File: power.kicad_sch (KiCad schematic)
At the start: 32 parts

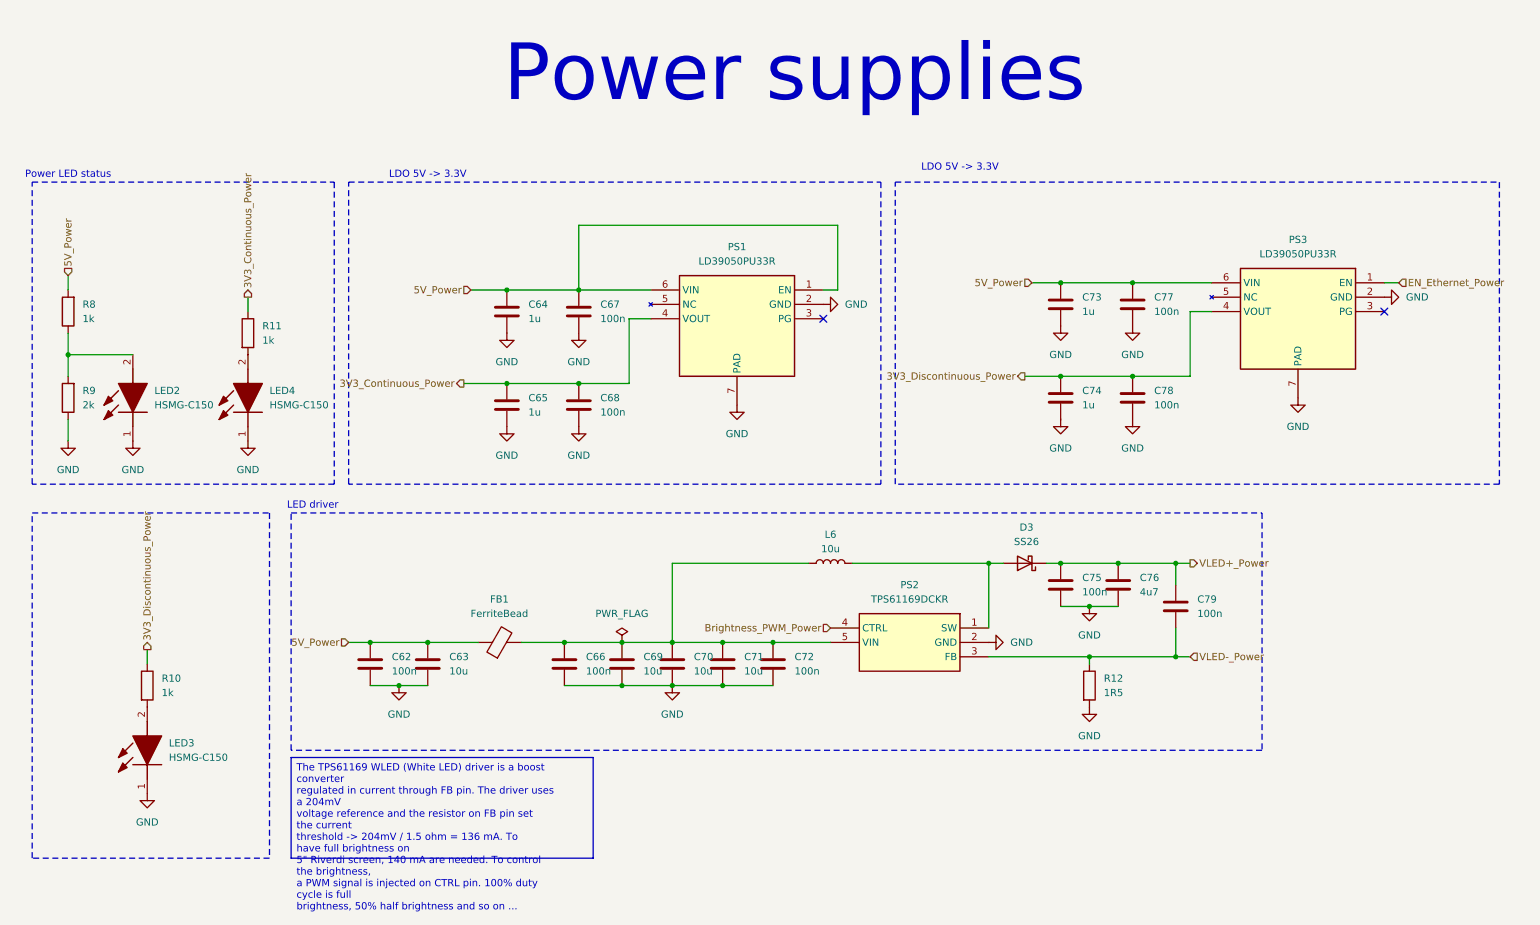
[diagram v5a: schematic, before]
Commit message: Remove Ethernet part, critical error, LAN8651 is 10BASE-T1S !
10BASE-T1S is not suitable with RJ45 connector and not connectable to computer
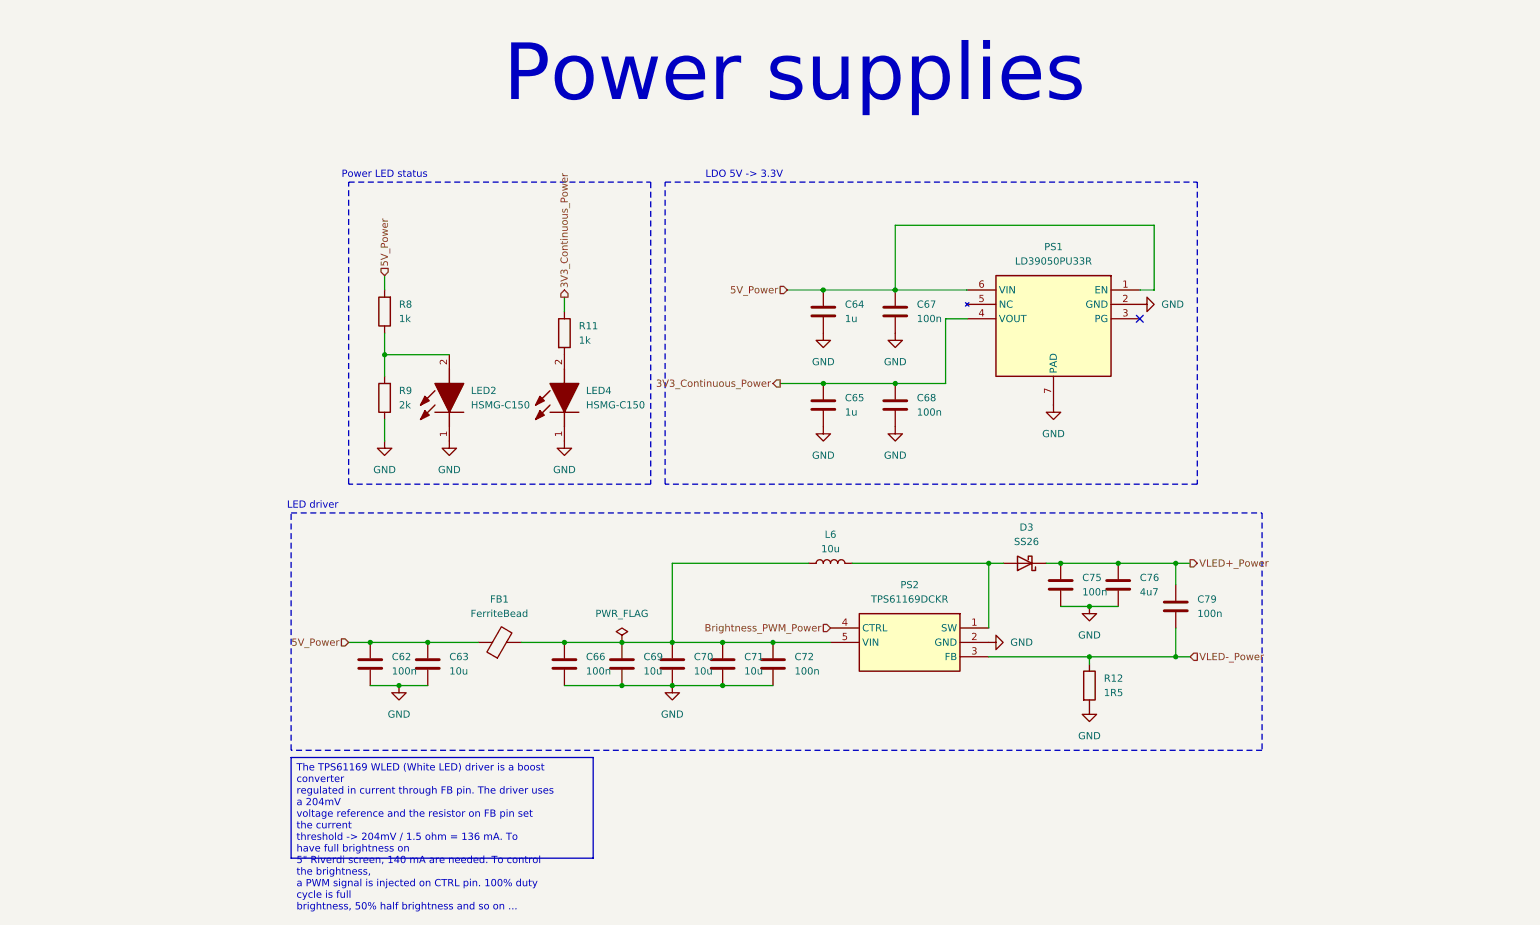
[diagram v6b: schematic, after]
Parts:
- removed C73, C74: 1u, symbol Device:C
- removed C77, C78: 100n, symbol Device:C
- removed LED3: HSMG-C150, weather-station-poc-fp:LEDC3216X120N, symbol weather-station-poc-sym:HSMG-C150
- removed PS3: LD39050PU33R, weather-station-poc-fp:SON95P300X300X100-7N-D, symbol weather-station-poc-sym:LD39050PU33R
- removed R10: 1k, symbol Device:R
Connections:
- no-connect marks 2 -> 1
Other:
- moved on the sheet: C64, C65, C67, C68, LED2, LED4, PS1, R11, R8, R9

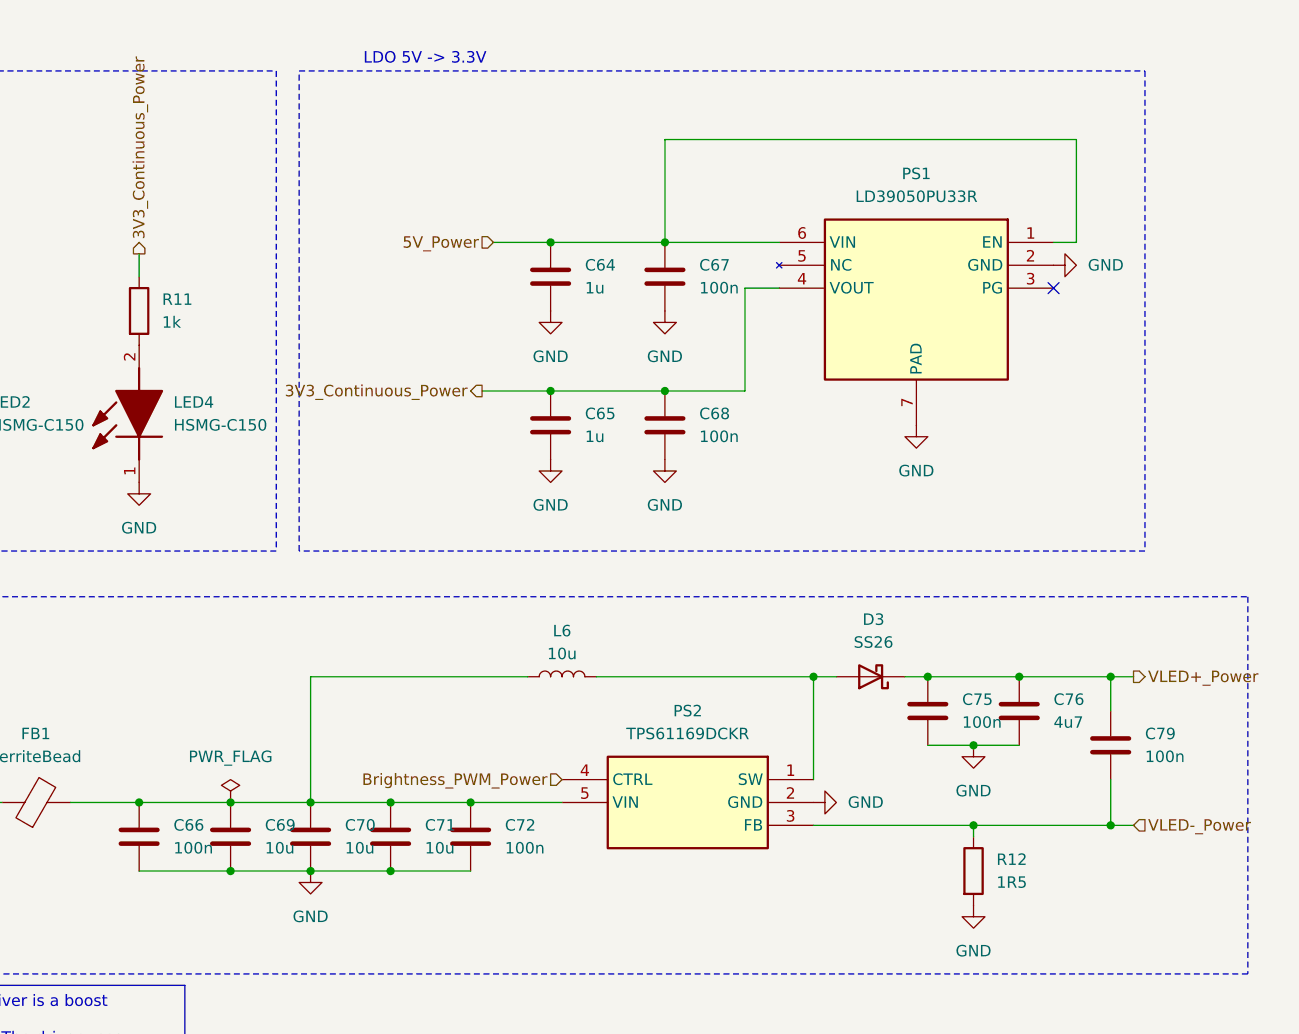
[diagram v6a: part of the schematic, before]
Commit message: Reorder components number
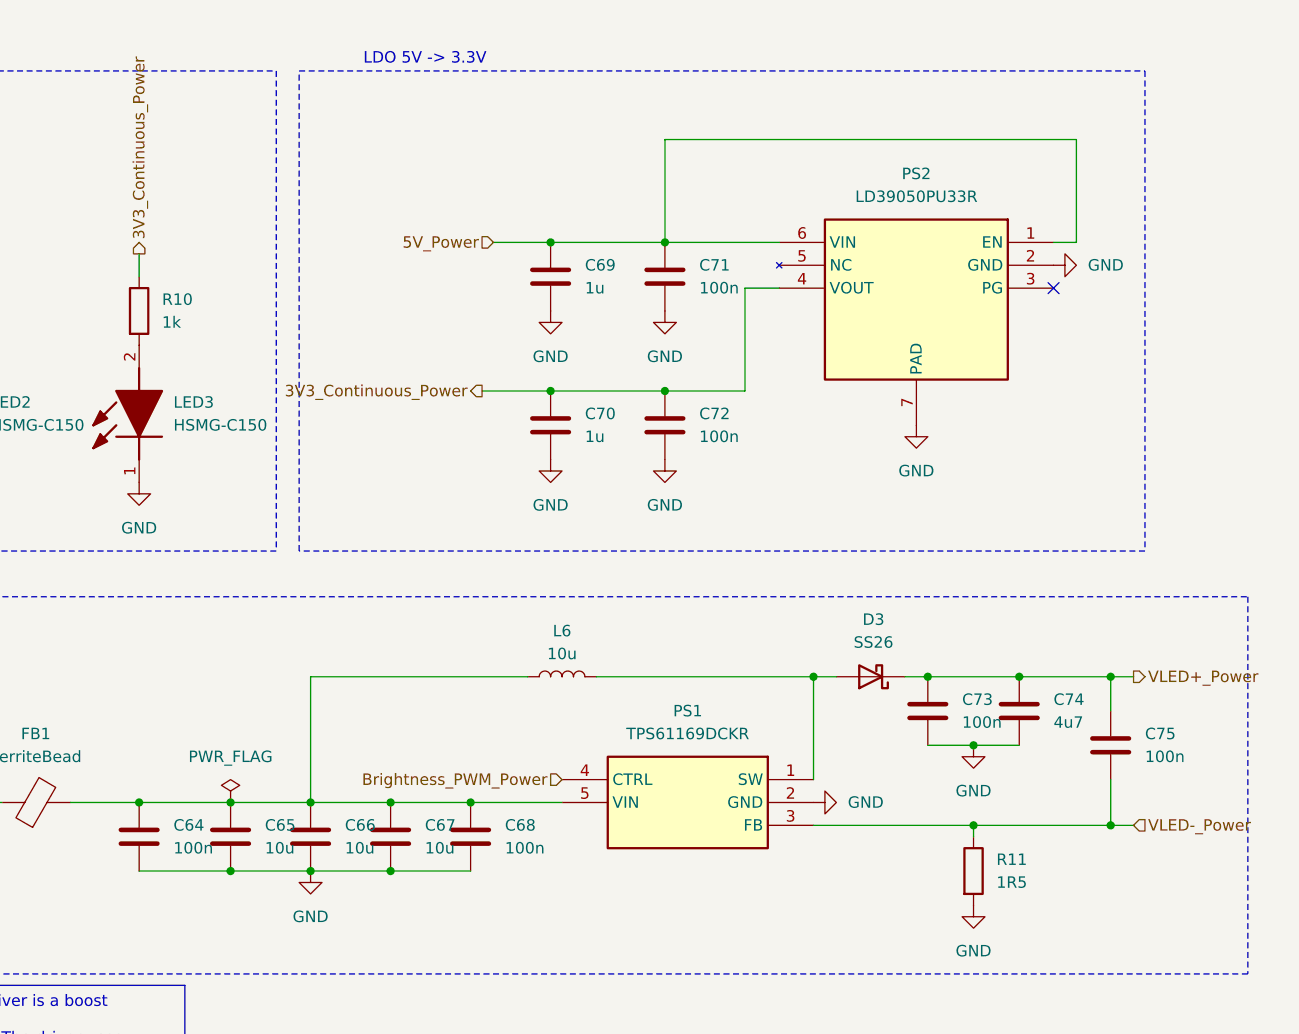
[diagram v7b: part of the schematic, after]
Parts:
- renumbered C66 to C64, C69 to C65, C70 to C66, C71 to C67, C72 to C68, C64 to C69, C65 to C70, C67 to C71, C68 to C72, C75 to C73, C76 to C74, C79 to C75, LED4 to LED3, PS2 to PS1, PS1 to PS2, R11 to R10, R12 to R11

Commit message: Assign 0603 footprint to all capacitors
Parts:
- C62, C63, C64, C65, C67, C68, C69, C70, C71, C72, C73, C74, C75: footprint (none) -> Capacitor_SMD:C_0603_1608Metric_Pad1.08x0.95mm_HandSolder
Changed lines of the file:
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@@
 			)
 		)
-		(property "Footprint" ""
+		(property "Footprint" "Capacitor_SMD:C_0603_1608Metric_Pad1.08x0.95mm_HandSolder"
 			(at 201.6252 118.11 0)
 			(effects
@@
 			)
 		)
-		(property "Footprint" ""
+		(property "Footprint" "Capacitor_SMD:C_0603_1608Metric_Pad1.08x0.95mm_HandSolder"
 			(at 159.7152 69.85 0)
 			(effects
@@
 			)
 		)
-		(property "Footprint" ""
+		(property "Footprint" "Capacitor_SMD:C_0603_1608Metric_Pad1.08x0.95mm_HandSolder"
 			(at 89.8652 132.08 0)
 			(effects
@@
 			)
 		)
-		(property "Footprint" ""
+		(property "Footprint" "Capacitor_SMD:C_0603_1608Metric_Pad1.08x0.95mm_HandSolder"
 			(at 79.7052 132.08 0)
 			(effects
@@
 			)
 		)
-		(property "Footprint" ""
+		(property "Footprint" "Capacitor_SMD:C_0603_1608Metric_Pad1.08x0.95mm_HandSolder"
 			(at 150.8252 132.08 0)
 			(effects
@@
 			)
 		)
-		(property "Footprint" ""
+		(property "Footprint" "Capacitor_SMD:C_0603_1608Metric_Pad1.08x0.95mm_HandSolder"
 			(at 221.9452 121.92 0)
 			(effects
@@
 			)
 		)
-		(property "Footprint" ""
+		(property "Footprint" "Capacitor_SMD:C_0603_1608Metric_Pad1.08x0.95mm_HandSolder"
 			(at 159.7152 86.36 0)
 			(effects
@@
 			)
 		)
-		(property "Footprint" ""
+		(property "Footprint" "Capacitor_SMD:C_0603_1608Metric_Pad1.08x0.95mm_HandSolder"
 			(at 172.4152 86.36 0)
 			(effects
@@
 			)
 		)
-		(property "Footprint" ""
+		(property "Footprint" "Capacitor_SMD:C_0603_1608Metric_Pad1.08x0.95mm_HandSolder"
 			(at 124.1552 132.08 0)
 			(effects
@@
 			)
 		)
-		(property "Footprint" ""
+		(property "Footprint" "Capacitor_SMD:C_0603_1608Metric_Pad1.08x0.95mm_HandSolder"
 			(at 172.4152 69.85 0)
 			(effects
@@
 			)
 		)
-		(property "Footprint" ""
+		(property "Footprint" "Capacitor_SMD:C_0603_1608Metric_Pad1.08x0.95mm_HandSolder"
 			(at 141.9352 132.08 0)
 			(effects
@@
 			)
 		)
-		(property "Footprint" ""
+		(property "Footprint" "Capacitor_SMD:C_0603_1608Metric_Pad1.08x0.95mm_HandSolder"
 			(at 113.9952 132.08 0)
 			(effects
@@
 			)
 		)
-		(property "Footprint" ""
+		(property "Footprint" "Capacitor_SMD:C_0603_1608Metric_Pad1.08x0.95mm_HandSolder"
 			(at 211.7852 118.11 0)
 			(effects
